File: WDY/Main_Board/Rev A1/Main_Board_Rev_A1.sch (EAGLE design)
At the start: 201 parts, among them J1 22-05-7028-02, J10 22-05-7038-03, J11 FTSH-105-01-L-DV, J12 22-05-7028-02, J13 22-05-7028-02, J14 22-05-7028-02, J15 22-05-7058-05, J16 22-27-2061-06, J17 22-05-7048-04, J2 22-05-7028-02, J3 22-05-7048-04, J4 22-05-7048-04, J5 1241050-5, J6 90814-0208, J7 90814-0206, J8 90814-0208, J9 22-05-7038-03, K1 G6K-2G-Y, K2 G6K-2G-Y, K3 G6K-2G-Y, K4 G6K-2G-Y, P1 RB1-125BAG1A, SW1 B3FS-1015, SW2 B3FS-1015, T1 MMBT2222AL, U1 LPC1768FBD100, U10 TLV313, U11 SN74LVC3G17DCTR, U2 SN74LVC3G17DCTR, U3 SN74LVC3G17DCTR, U4 TPL0401A, U5 AT24C512C-SSHM-B, U6 SN74LVC2G17DBVR, U7 SN74LVC2G17DBVR, U8 LT1767EMS8E-5PBF, U9 TC1264-3.3, X1 FC-135, X2 MSTBA2

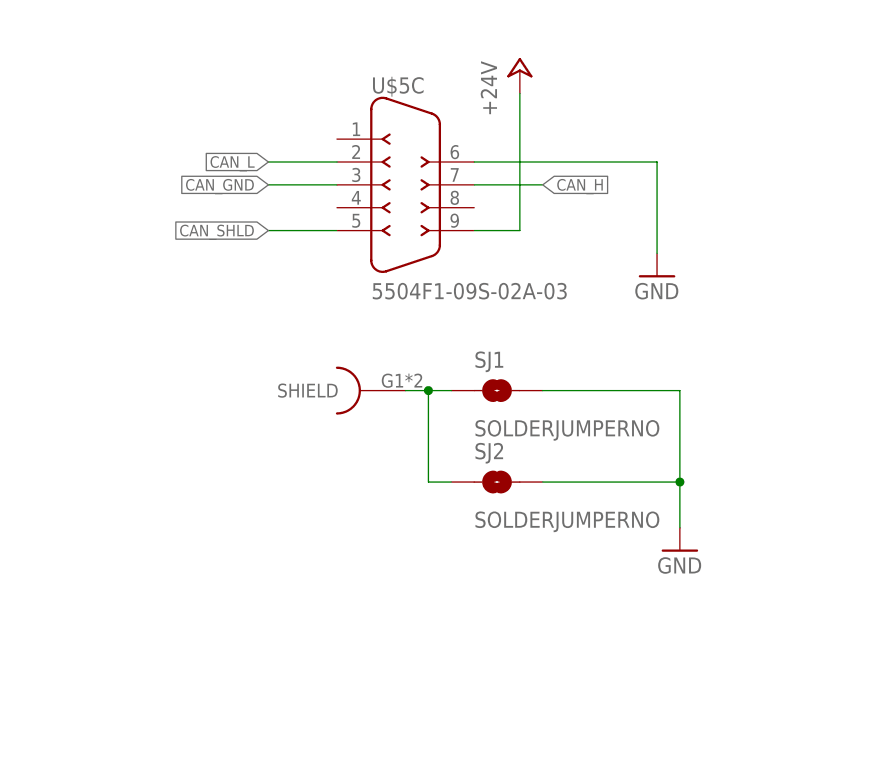
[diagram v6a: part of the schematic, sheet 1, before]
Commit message: Connect CAN_GND to GND
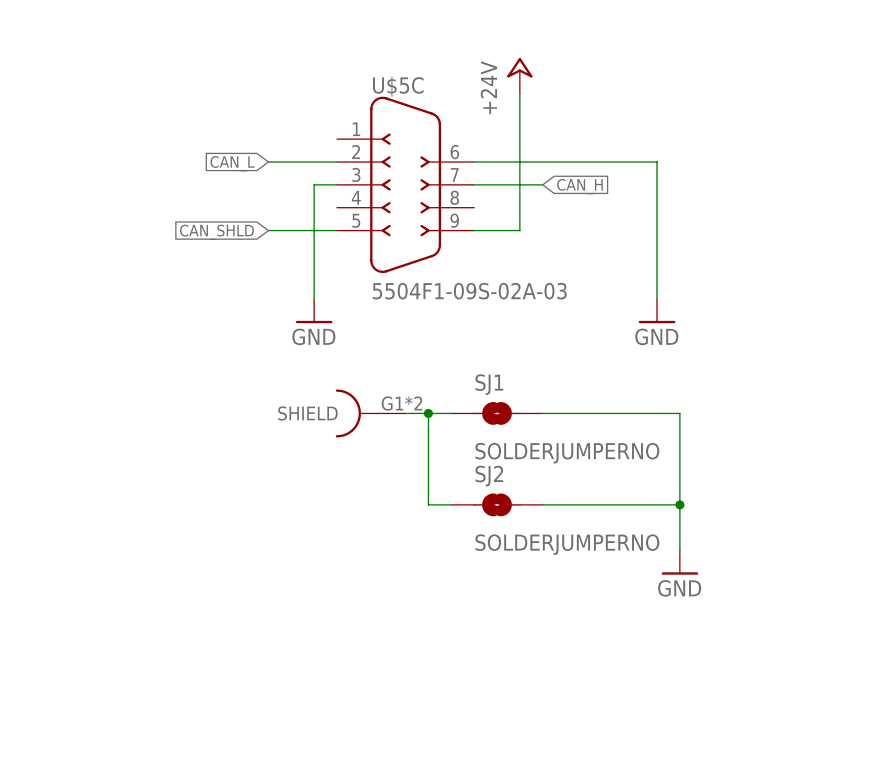
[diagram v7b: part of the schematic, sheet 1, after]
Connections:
- removed net CAN_GND: U$5C.3
- net GND: now also U$5C.3
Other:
- moved on the sheet: SJ1, SJ2
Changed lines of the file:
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@@
 <part name="SJ3" library="SparkFun-Passives" deviceset="SOLDERJUMPER" device="NO"/>
 <part name="P+23" library="supply1" deviceset="+5V" device=""/>
+<part name="GND92" library="supply1" deviceset="GND" device=""/>
 </parts>
 <sheets>
@@
 <instance part="R10" gate="G$1" x="198.12" y="60.96"/>
 <instance part="U$5" gate="C" x="83.82" y="71.12"/>
-<instance part="GND18" gate="1" x="111.76" y="60.96"/>
-<instance part="U$5" gate="S" x="81.28" y="48.26" rot="R90"/>
-<instance part="SJ1" gate="1" x="93.98" y="48.26"/>
-<instance part="SJ2" gate="1" x="93.98" y="38.1"/>
-<instance part="GND19" gate="1" x="114.3" y="30.48"/>
+<instance part="GND18" gate="1" x="111.76" y="55.88"/>
+<instance part="U$5" gate="S" x="81.28" y="45.72" rot="R90"/>
+<instance part="SJ1" gate="1" x="93.98" y="45.72"/>
+<instance part="SJ2" gate="1" x="93.98" y="35.56"/>
+<instance part="GND19" gate="1" x="114.3" y="27.94"/>
 <instance part="J14" gate="-1" x="25.4" y="139.7" rot="MR0"/>
 <instance part="J14" gate="-2" x="25.4" y="134.62" rot="MR0"/>
@@
 <instance part="JP4" gate="G$1" x="352.298" y="21.59"/>
 <instance part="JP5" gate="G$1" x="356.362" y="21.59"/>
+<instance part="GND92" gate="1" x="73.66" y="55.88"/>
 </instances>
 <busses>
@@
 <pinref part="GND18" gate="1" pin="GND"/>
 <wire x1="91.44" y1="73.66" x2="111.76" y2="73.66" width="0.1524" layer="91"/>
-<wire x1="111.76" y1="73.66" x2="111.76" y2="63.5" width="0.1524" layer="91"/>
+<wire x1="111.76" y1="73.66" x2="111.76" y2="58.42" width="0.1524" layer="91"/>
 </segment>
 <segment>
 <pinref part="SJ1" gate="1" pin="2"/>
-<wire x1="99.06" y1="48.26" x2="114.3" y2="48.26" width="0.1524" layer="91"/>
+<wire x1="99.06" y1="45.72" x2="114.3" y2="45.72" width="0.1524" layer="91"/>
 <pinref part="GND19" gate="1" pin="GND"/>
-<wire x1="114.3" y1="33.02" x2="114.3" y2="38.1" width="0.1524" layer="91"/>
+<wire x1="114.3" y1="30.48" x2="114.3" y2="35.56" width="0.1524" layer="91"/>
 <pinref part="SJ2" gate="1" pin="2"/>
-<wire x1="114.3" y1="38.1" x2="114.3" y2="48.26" width="0.1524" layer="91"/>
-<wire x1="99.06" y1="38.1" x2="114.3" y2="38.1" width="0.1524" layer="91"/>
-<junction x="114.3" y="38.1"/>
+<wire x1="114.3" y1="35.56" x2="114.3" y2="45.72" width="0.1524" layer="91"/>
+<wire x1="99.06" y1="35.56" x2="114.3" y2="35.56" width="0.1524" layer="91"/>
+<junction x="114.3" y="35.56"/>
 </segment>
 <segment>
@@
 <wire x1="27.94" y1="134.62" x2="35.56" y2="134.62" width="0.1524" layer="91"/>
 <wire x1="35.56" y1="134.62" x2="35.56" y2="132.08" width="0.1524" layer="91"/>
+</segment>
+<segment>
+<pinref part="U$5" gate="C" pin="3"/>
+<wire x1="76.2" y1="71.12" x2="73.66" y2="71.12" width="0.1524" layer="91"/>
+<pinref part="GND92" gate="1" pin="GND"/>
+<wire x1="73.66" y1="58.42" x2="73.66" y2="71.12" width="0.1524" layer="91"/>
 </segment>
 </net>
@@
 </segment>
 </net>
-<net name="CAN_GND" class="0">
-<segment>
-<pinref part="U$5" gate="C" pin="3"/>
-<wire x1="76.2" y1="71.12" x2="68.58" y2="71.12" width="0.1524" layer="91"/>
-<label x="68.58" y="71.12" size="1.27" layer="95" rot="R180" xref="yes"/>
-</segment>
-</net>
 <net name="CAN_SHLD" class="0">
 <segment>
@@
 <pinref part="U$5" gate="S" pin="SHIELD"/>
 <pinref part="SJ1" gate="1" pin="1"/>
-<wire x1="83.82" y1="48.26" x2="86.36" y2="48.26" width="0.1524" layer="91"/>
+<wire x1="83.82" y1="45.72" x2="86.36" y2="45.72" width="0.1524" layer="91"/>
 <pinref part="SJ2" gate="1" pin="1"/>
-<wire x1="86.36" y1="48.26" x2="88.9" y2="48.26" width="0.1524" layer="91"/>
-<wire x1="86.36" y1="48.26" x2="86.36" y2="38.1" width="0.1524" layer="91"/>
-<wire x1="86.36" y1="38.1" x2="88.9" y2="38.1" width="0.1524" layer="91"/>
-<junction x="86.36" y="48.26"/>
-</segment>
-</net>
+<wire x1="86.36" y1="45.72" x2="88.9" y2="45.72" width="0.1524" layer="91"/>
+<wire x1="86.36" y1="45.72" x2="86.36" y2="35.56" width="0.1524" layer="91"/>
+<wire x1="86.36" y1="35.56" x2="88.9" y2="35.56" width="0.1524" layer="91"/>
+<junction x="86.36" y="45.72"/>
+</segment>
+</net>
